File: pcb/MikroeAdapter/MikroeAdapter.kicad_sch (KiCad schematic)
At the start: 19 parts, among them CON1 MIKROBUS_HOST_CONN, J1 Screw_Terminal_01x02, J2 Conn_01x03, J3 Conn_01x02, J4 Screw_Terminal_01x12, J5 Screw_Terminal_01x02, U1 ATtiny1604-SS, U2 HT75xx-1-SOT89, U3 THVD1450D

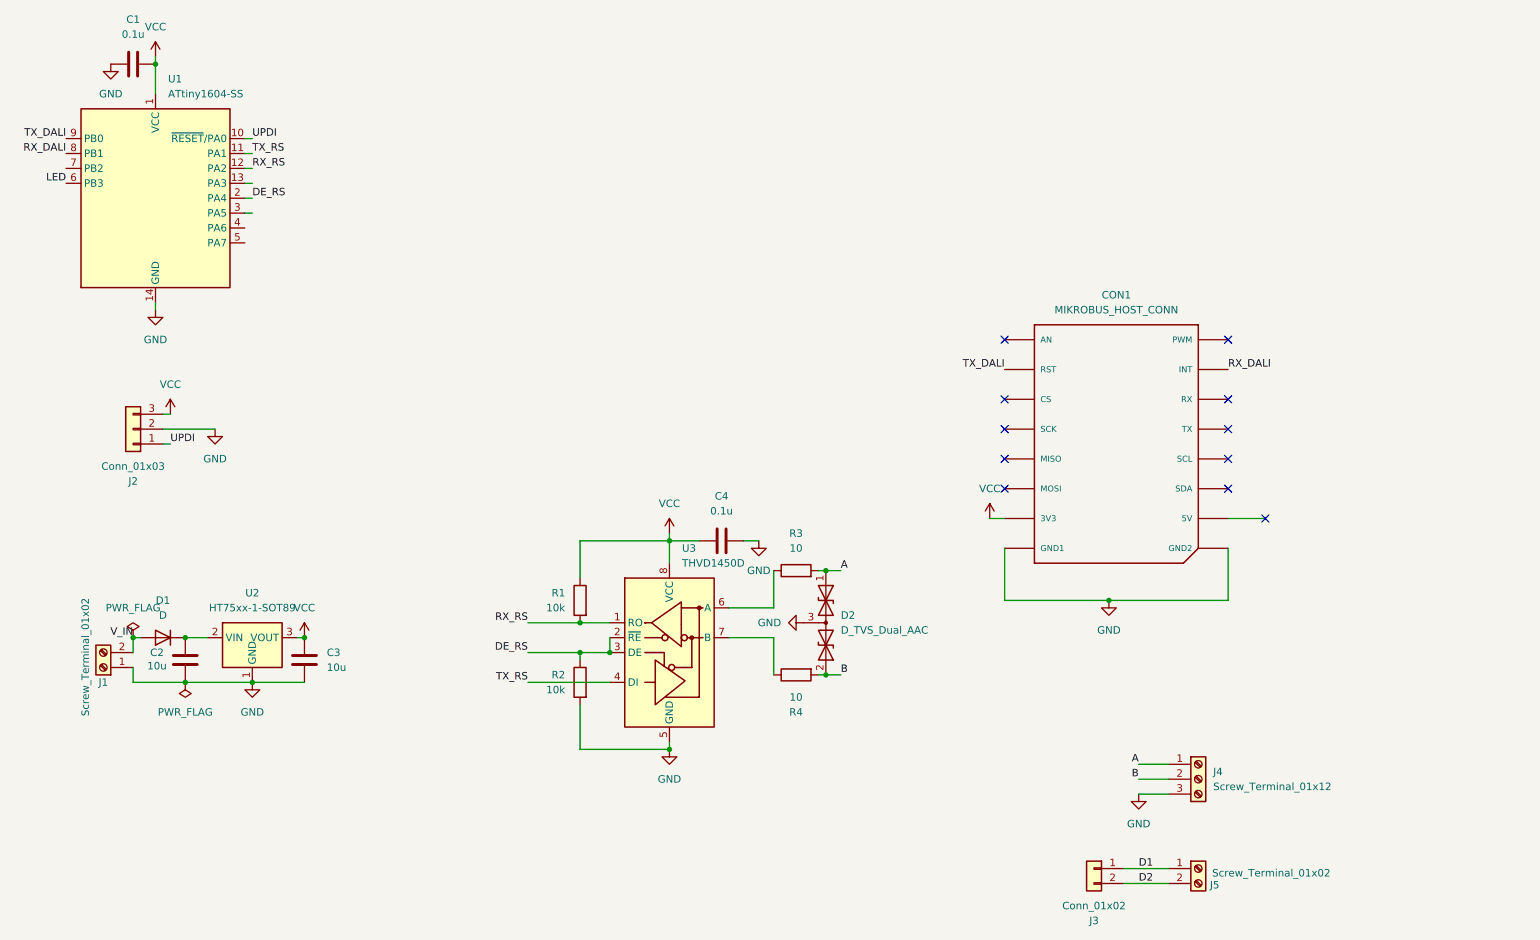
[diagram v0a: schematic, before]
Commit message: Switched to buck converter for power so that we can run effectively off 12V
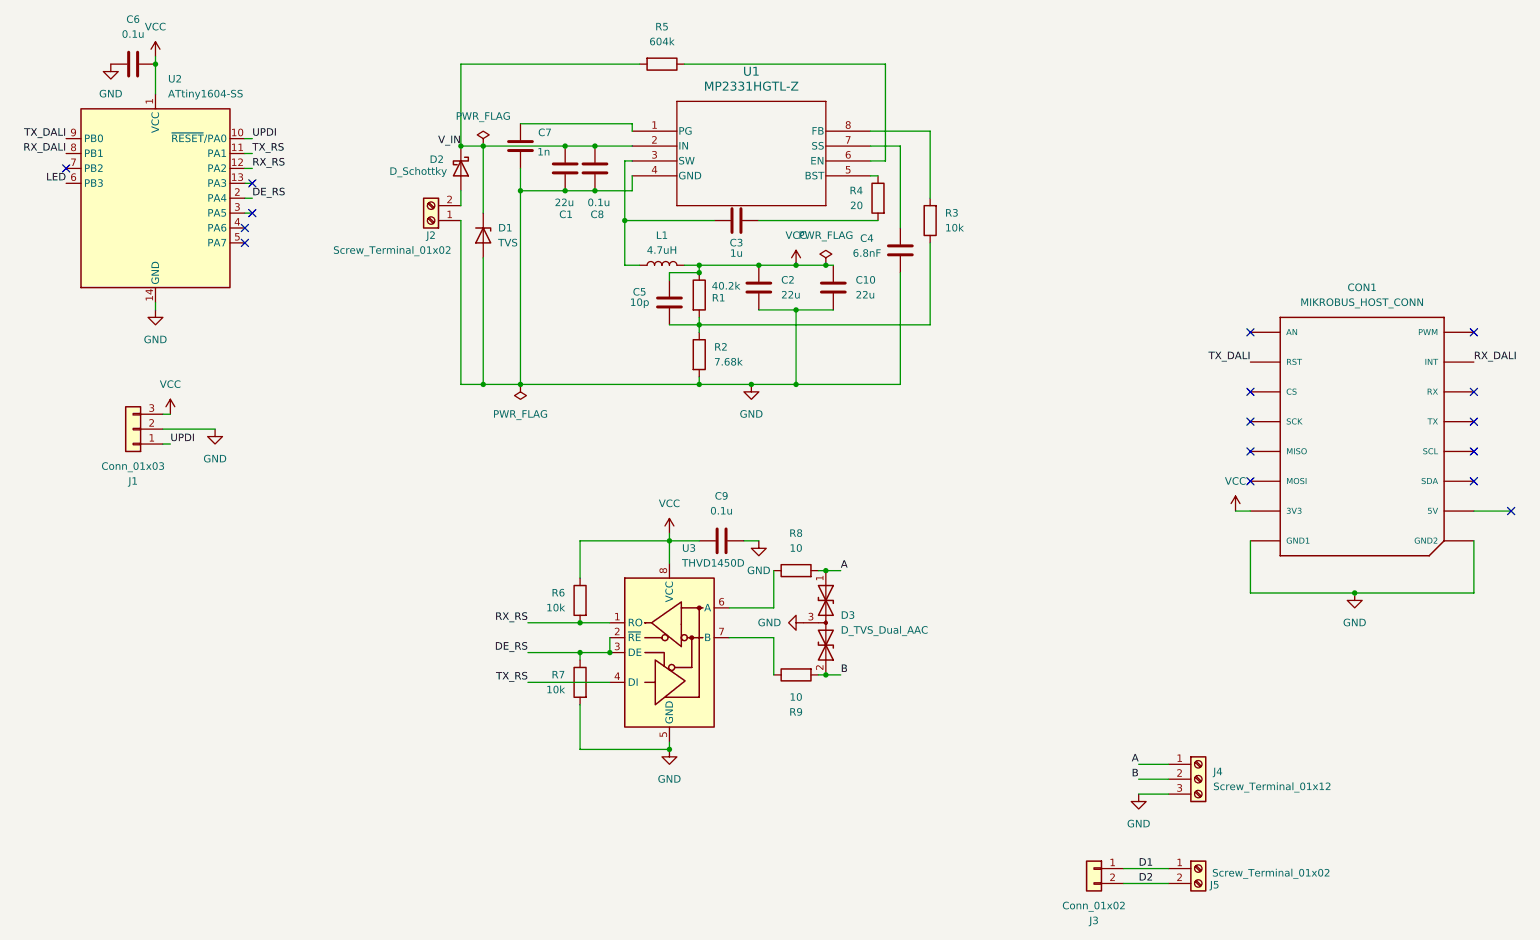
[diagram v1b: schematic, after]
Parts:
- removed D1: D, Diode_SMD:D_SOD-123F, symbol Device:D
- removed U2: HT75xx-1-SOT89, Package_TO_SOT_SMD:SOT-89-3, symbol Regulator_Linear:HT75xx-1-SOT89
- added C1, C10: 22u, Capacitor_SMD:C_1210_3225Metric, symbol Device:C
- added C4: 6.8nF, Capacitor_SMD:C_0603_1608Metric, symbol Device:C
- added C5: 10p, Capacitor_SMD:C_0402_1005Metric, symbol Device:C
- added C7: 1n, Capacitor_SMD:C_0402_1005Metric, symbol Device:C
- added C8: 0.1u, Capacitor_SMD:C_0402_1005Metric, symbol Device:C
- added D1: TVS, Diode_SMD:D_SMB, symbol Device:D_Zener
- added D2: D_Schottky, Diode_SMD:D_SMA, symbol Device:D_Schottky
- added L1: 4.7uH, FNR4030:IND-SMD_L4.0-W4.0_FNR40XXS, symbol Device:L
- added R1: 40.2k, Resistor_SMD:R_0402_1005Metric, symbol Device:R
- added R2: 7.68k, Resistor_SMD:R_0402_1005Metric, symbol Device:R
- added R3: 10k, Resistor_SMD:R_0402_1005Metric, symbol Device:R
- added R4: 20, Resistor_SMD:R_0402_1005Metric, symbol Device:R
- added R5: 604k, Resistor_SMD:R_0402_1005Metric, symbol Device:R
- added U1: MP2331HGTL-Z, Package_TO_SOT_SMD:SOT-583-8, symbol MP2331:MP2331HGTL-Z
- C2: value 10u -> 22u; footprint Capacitor_SMD:C_0805_2012Metric -> Capacitor_SMD:C_1210_3225Metric
- C3: value 10u -> 1u; footprint Capacitor_SMD:C_0805_2012Metric -> Capacitor_SMD:C_0603_1608Metric
- C9: renamed from C4; footprint Capacitor_SMD:C_0805_2012Metric -> Capacitor_SMD:C_0402_1005Metric
- renumbered C1 to C6, D2 to D3, J2 to J1, J1 to J2, R1 to R6, R2 to R7, R3 to R8, R4 to R9, U1 to U2
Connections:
- net GND: now also C1.2, C10.2, C4.1, C7.2, C8.2, D1.2 (A), R2.2, U1.4 (GND); no longer C3.2
- net VCC: now also C2.1, C10.1, C5.1, L1.2, R1.1; no longer C3.1
- net V_IN: now also C1.1, C8.1, D1.1 (K), D2.1 (K), R5.2, U1.2 (IN); no longer J2.2 (Pin_2)
- new net: C3.2, L1.1, U1.3 (SW)
- new net: D2.2 (A), J2.2 (Pin_2)
- new net: C5.2, R1.2, R2.1, R3.1
- new net: C4.2, U1.7 (SS)
- new net: C3.1, R4.2
- new net: R5.1, U1.6 (EN)
- new net: R4.1, U1.5 (BST)
- new net: C7.1, U1.1 (PG)
- new net: R3.2, U1.8 (FB)
- no-connect marks 11 -> 16
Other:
- moved on the sheet: CON1, J2
